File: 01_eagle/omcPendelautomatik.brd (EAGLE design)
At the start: 44.5 x 69.8 mm, 71 parts, among them IC1 PIC12F675, IC2 7805, IC3 L5970D, K1 NA-5V, T1 BSS138, T2 BSS138, X1 RT034 Typ 086, X2 2X3

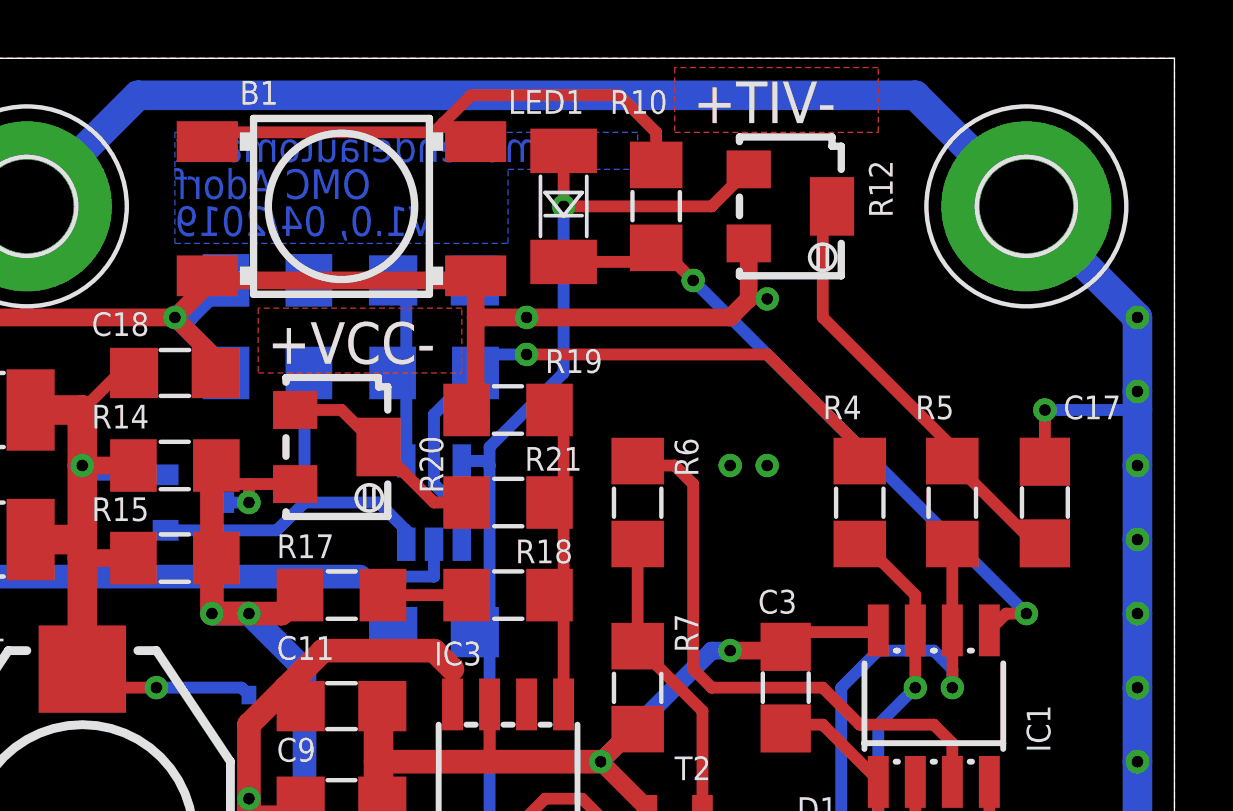
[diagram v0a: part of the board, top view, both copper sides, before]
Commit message: bugfix uC button wiring
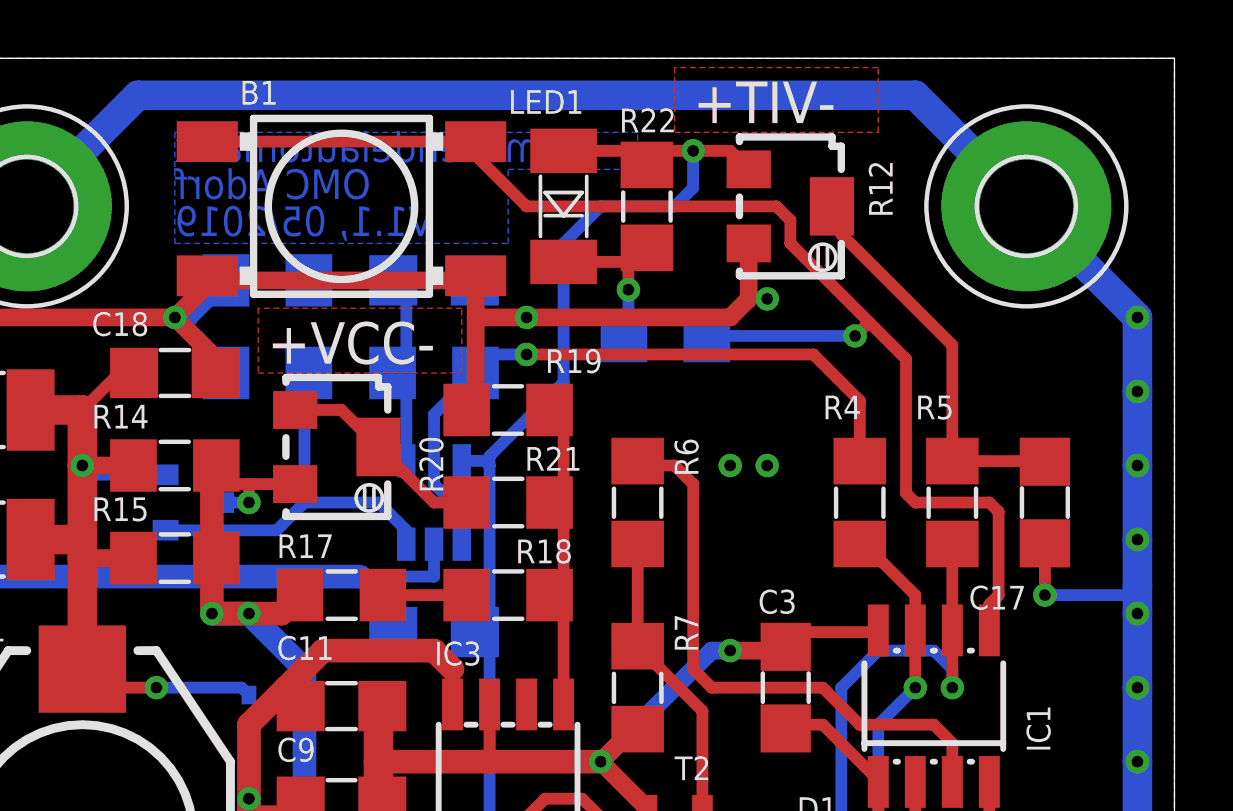
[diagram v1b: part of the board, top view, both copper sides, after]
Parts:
- added R22: 56K, omcResistor:1206
- moved R10 4.46 mm to (27.0, 60.3), flipped to the bottom, turned to 0 degrees
- turned C17 to 270 degrees
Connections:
- removed net N$28: B1.3, B1.4, R10.1
- new net N$32: LED1.2, R10.2, R22.1
- net +5V: now also R22.2
- net N$27: now also B1.3, B1.4, R10.1; no longer LED1.2, R10.2
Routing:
- net N$27: track 23.1 -> 46.0 mm, vias 2 -> 1
- net N$28: track 19.1 -> 0.00 mm
- net N$32: track 0.00 -> 5.66 mm, vias 0 -> 1
- net +5V: track 108.9 -> 112.5 mm
- net I_VCC: track 25.0 -> 26.5 mm
- net N$19: track 15.1 -> 14.1 mm
- net GND: track 449.3 -> 448.8 mm
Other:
- board text added: "V1.1, 05/2019"
- board text removed: "V1.0, 04/2019"

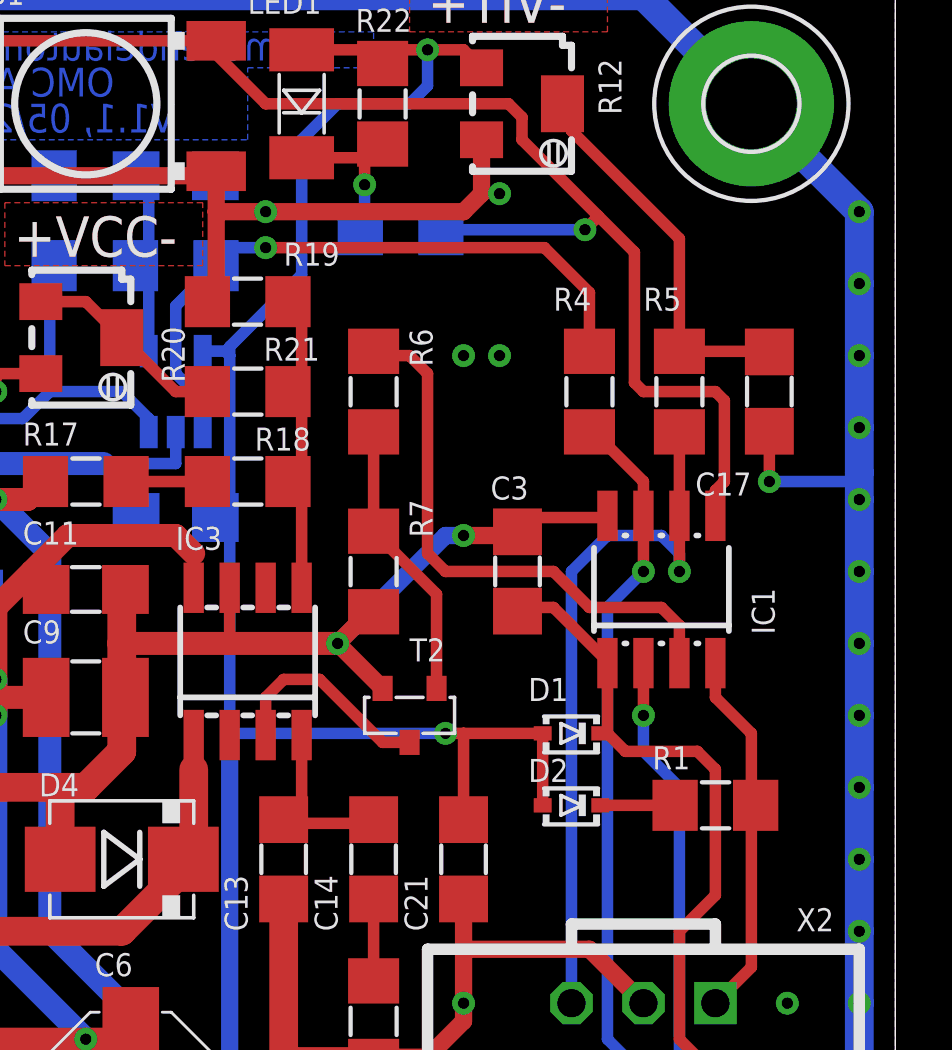
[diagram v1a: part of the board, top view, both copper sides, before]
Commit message: added tank caps for current sense adc, pcb done
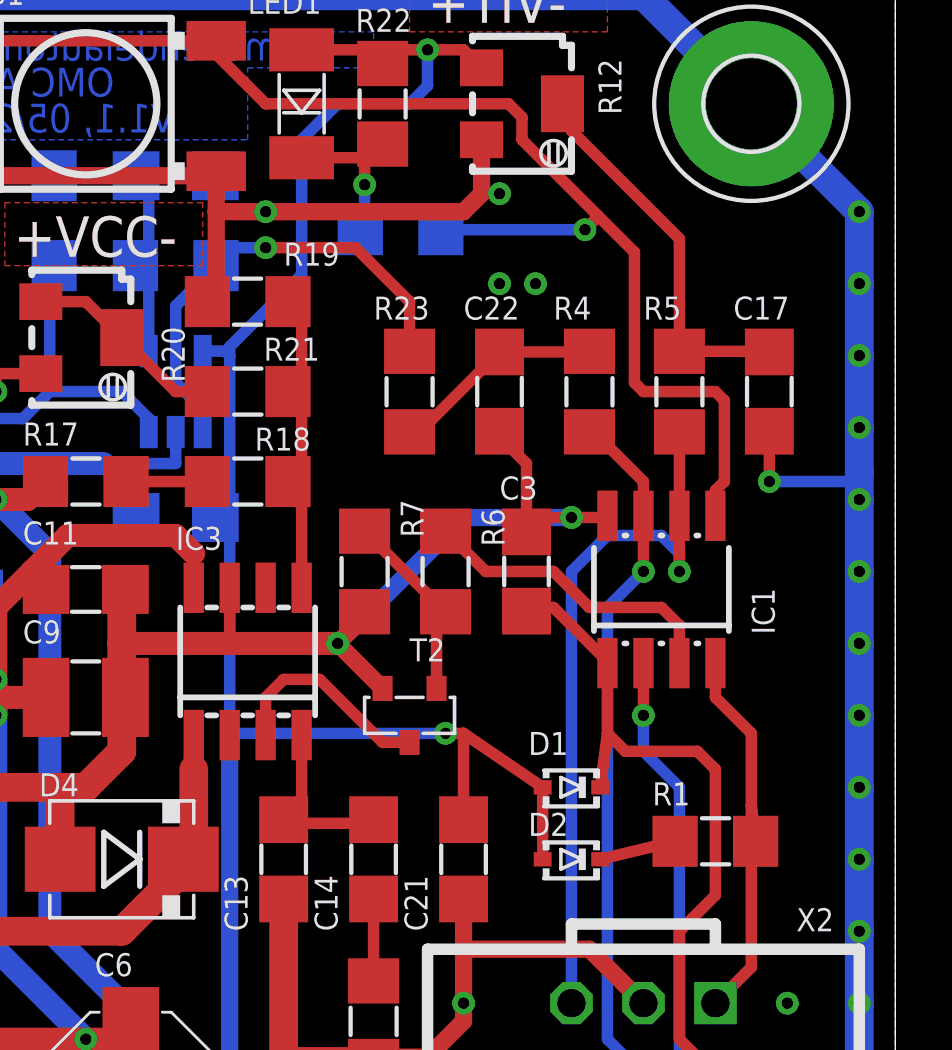
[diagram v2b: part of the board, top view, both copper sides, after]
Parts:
- added C22: 220n/50V, omcCapacitor:1206
- added R23: 200R, omcResistor:1206
- C15, C21: value 100n -> 100n/50V
- C17: value 100n/50V -> 220n/50V
- moved R6 6.84 mm to (28.6, 48.3)
- moved D1 1.91 mm to (33.0, 40.6)
- moved D2 1.91 mm to (33.0, 38.1)
- moved R1 1.27 mm to (38.1, 38.7)
- moved C3 0.32 mm to (31.4, 48.3)
- moved R7 0.32 mm to (25.7, 48.3)
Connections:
- new net N$33: C16.2, OPA1.1, R11.2, R23.2
- net GND: now also C22.2
- net I_VCC: now also C22.1, R23.1; no longer C16.2, OPA1.1, R11.2
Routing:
- net N$33: track 0.00 -> 19.7 mm, vias 0 -> 1
- net I_VCC: track 26.5 -> 8.01 mm, vias 1 -> 0
- net N$14: track 19.9 -> 11.0 mm
- net GND: track 448.8 -> 454.6 mm
- net N$13: track 10.5 -> 7.66 mm
- net N$7: track 23.0 -> 24.7 mm
- net N$10: track 13.2 -> 14.3 mm
- net +5V: track 112.5 -> 113.1 mm
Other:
- board text added: "https://github.com/akaeba/omcPendelautomatik"
